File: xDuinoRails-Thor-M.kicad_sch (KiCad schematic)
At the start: 1 part, among them U1101 MOUDLE-SEEEDUINO-XIAO

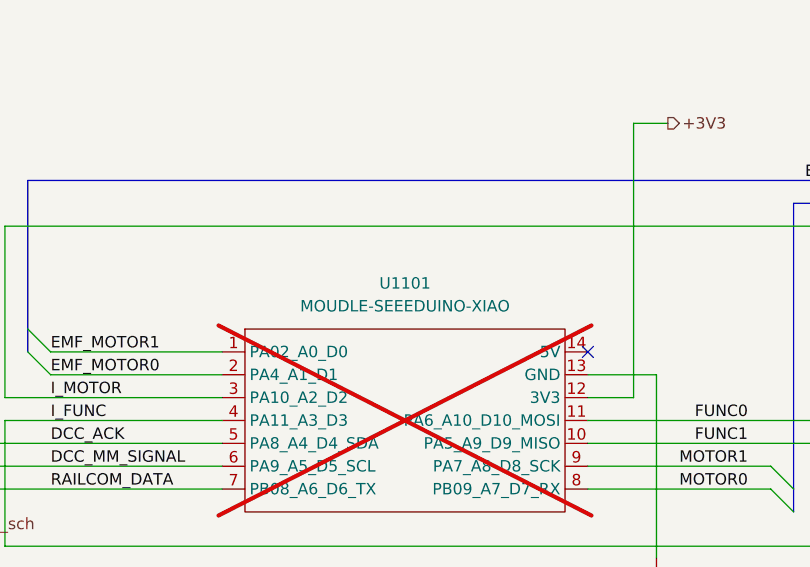
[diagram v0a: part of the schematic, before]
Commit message: Add - New annotations of schematics
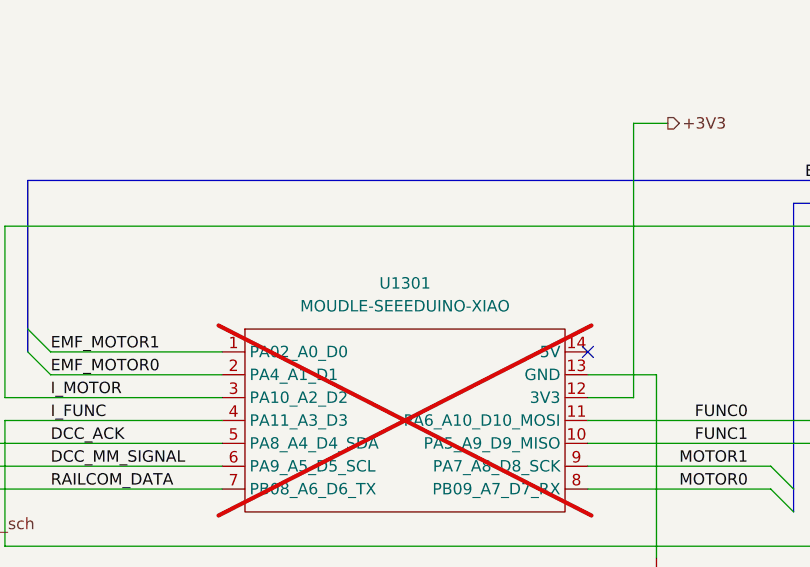
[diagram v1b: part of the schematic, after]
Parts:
- renumbered U1101 to U1301
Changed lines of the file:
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@@
 		(dnp no)
 		(fields_autoplaced yes)
-		(property "Reference" "#PWR1105"
+		(property "Reference" "#PWR1305"
 			(at 248.92 133.35 0)
 			(effects
@@
 			(project "xDuinoRails-Thor-M"
 				(path "/fb33ec4e-6596-45d2-a121-8d3475acd69a"
-					(reference "#PWR1105")
+					(reference "#PWR1305")
 					(unit 1)
 				)
@@
 		(dnp no)
 		(fields_autoplaced yes)
-		(property "Reference" "#PWR1108"
+		(property "Reference" "#PWR1308"
 			(at 187.96 157.48 0)
 			(effects
@@
 			(project "xDuinoRails-Thor-M"
 				(path "/fb33ec4e-6596-45d2-a121-8d3475acd69a"
-					(reference "#PWR1108")
+					(reference "#PWR1308")
 					(unit 1)
 				)
@@
 		(dnp no)
 		(fields_autoplaced yes)
-		(property "Reference" "#PWR1104"
+		(property "Reference" "#PWR1304"
 			(at 180.34 120.65 0)
 			(effects
@@
 			(project "xDuinoRails-Thor-M"
 				(path "/fb33ec4e-6596-45d2-a121-8d3475acd69a"
-					(reference "#PWR1104")
+					(reference "#PWR1304")
 					(unit 1)
 				)
@@
 		(dnp no)
 		(fields_autoplaced yes)
-		(property "Reference" "#PWR1102"
+		(property "Reference" "#PWR1302"
 			(at 44.45 72.39 0)
 			(effects
@@
 			(project "xDuinoRails-Hermes-M"
 				(path "/fb33ec4e-6596-45d2-a121-8d3475acd69a"
-					(reference "#PWR1102")
+					(reference "#PWR1302")
 					(unit 1)
 				)
@@
 		(dnp no)
 		(fields_autoplaced yes)
-		(property "Reference" "#PWR1103"
+		(property "Reference" "#PWR1303"
 			(at 144.78 72.39 0)
 			(effects
@@
 			(project "xDuinoRails-Hermes-M"
 				(path "/fb33ec4e-6596-45d2-a121-8d3475acd69a"
-					(reference "#PWR1103")
+					(reference "#PWR1303")
 					(unit 1)
 				)
@@
 		(dnp no)
 		(fields_autoplaced yes)
-		(property "Reference" "#PWR1106"
+		(property "Reference" "#PWR1306"
 			(at 34.29 144.78 0)
 			(effects
@@
 			(project "xDuinoRails-Hermes-M"
 				(path "/fb33ec4e-6596-45d2-a121-8d3475acd69a"
-					(reference "#PWR1106")
+					(reference "#PWR1306")
 					(unit 1)
 				)
@@
 		(dnp no)
 		(fields_autoplaced yes)
-		(property "Reference" "#PWR1101"
+		(property "Reference" "#PWR1301"
 			(at 100.33 71.12 0)
 			(effects
@@
 			(project "xDuinoRails-Thor-M"
 				(path "/fb33ec4e-6596-45d2-a121-8d3475acd69a"
-					(reference "#PWR1101")
+					(reference "#PWR1301")
 					(unit 1)
 				)
@@
 		(dnp yes)
 		(fields_autoplaced yes)
-		(property "Reference" "U1101"
+		(property "Reference" "U1301"
 			(at 109.22 107.95 0)
 			(effects
@@
 			(project ""
 				(path "/fb33ec4e-6596-45d2-a121-8d3475acd69a"
-					(reference "U1101")
+					(reference "U1301")
 					(unit 1)
 				)
@@
 		(dnp no)
 		(fields_autoplaced yes)
-		(property "Reference" "#PWR1107"
+		(property "Reference" "#PWR1307"
 			(at 137.16 144.78 0)
 			(effects
@@
 			(project "xDuinoRails-Hermes-S"
 				(path "/fb33ec4e-6596-45d2-a121-8d3475acd69a"
-					(reference "#PWR1107")
-					(unit 1)
-				)
+					(reference "#PWR1307")
+					(unit 1)
+				)
